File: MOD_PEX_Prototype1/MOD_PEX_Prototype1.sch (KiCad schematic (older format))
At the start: 66 parts, among them CN1 CONN_PANNEL_2X2, CN2 CONN_PANNEL_2X2, J1 RJ45_CHAIN, J2 RJ45_CHAIN, P1 HEADER_3X1, P2 HEADER_5X1, P3 HEADER_5X2, P4 HEADER_2X1, Q1 MMBT3904, Q2 MMBT3904, SW1 SWITCH_HH, U1 LPC111X_LQFP48, U2 AP1117E50G, U3 AP1117E33G, U4 SN75176BDR, X1 10MHz

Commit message: Created BOM with ITEAD template.
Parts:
- removed D2, D3: MMSZ5242B, SOD123, symbol ZENERSMALL
- added D2, D3: MMSZ5242B, SOD123, symbol ZENERsmall
- C1, C3, C7: value 10uF -> 100uF
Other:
- moved on the sheet: C15, C6, C9, CN1, CN2, J1, J2, P1, P3, P4, Q1, Q2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

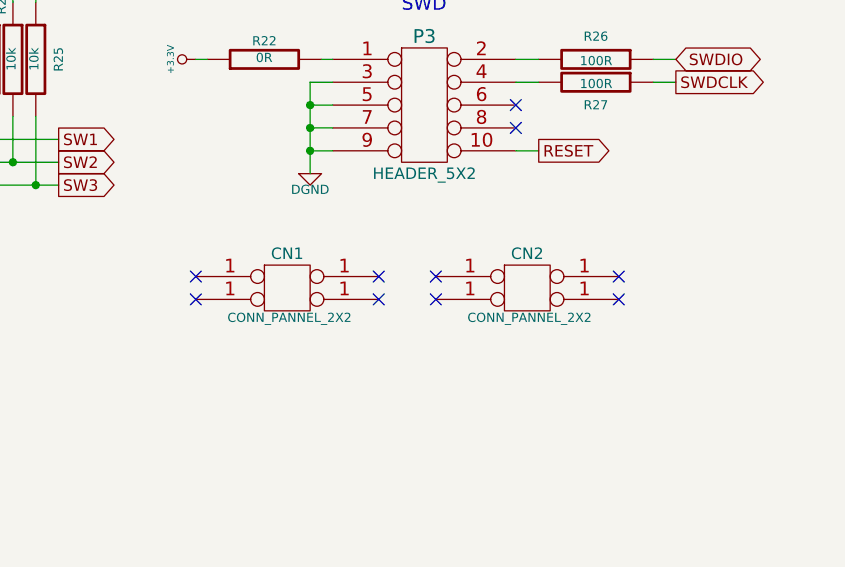
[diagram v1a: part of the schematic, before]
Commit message: Adding metadata to the schematics drawing (fix issue #5) and improving the PCB grounding by attaching CN1 and CN2 to the DGND copper plane (fix issue #4).
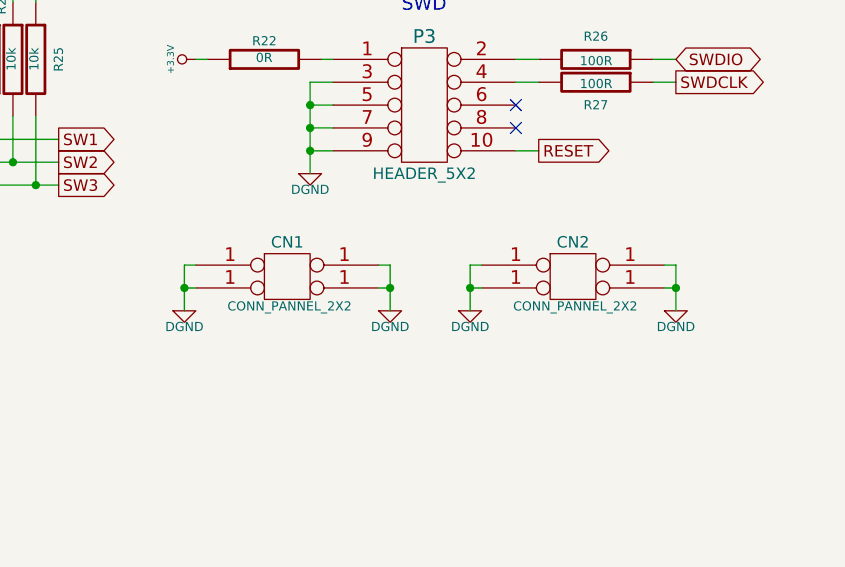
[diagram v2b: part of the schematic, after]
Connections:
- net DGND: now also CN1.1, CN2.1
- no-connect marks 39 -> 31
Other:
- moved on the sheet: CN1, CN2
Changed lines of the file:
@@
 LIBS:MOD_PEX_Prototype1
 LIBS:MOD_PEX_Prototype1-cache
-EELAYER 24 0
+EELAYER 25 0
 EELAYER END
 $Descr A4 11693 8268
 encoding utf-8
 Sheet 1 1
-Title ""
+Title "Control-Chain Expression Pedal for the MOD Project."
 Date "15 apr 2014"
 Rev ""
-Comp ""
+Comp "http://portalmod.com/"
 Comment1 ""
 Comment2 ""
@@
 	3500 1300 3500 1500
 Connection ~ 3500 1400
-NoConn ~ 9200 6250
-NoConn ~ 9200 6350
-NoConn ~ 8400 6250
-NoConn ~ 8400 6350
-NoConn ~ 10250 6250
-NoConn ~ 10250 6350
-NoConn ~ 9450 6250
-NoConn ~ 9450 6350
 $Comp
 L CONN_PANNEL_2X2 CN1
 U 1 1 534AEC1C
-P 8800 6300
-F 0 "CN1" H 8800 6450 50  0000 C CNN
-F 1 "CONN_PANNEL_2X2" H 8810 6170 40  0000 C CNN
-F 2 "CONN_PANNEL" H 8800 6300 60  0001 C CNN
-F 3 "" H 8800 6300 60  0000 C CNN
-	1    8800 6300
+P 8800 6250
+F 0 "CN1" H 8800 6400 50  0000 C CNN
+F 1 "CONN_PANNEL_2X2" H 8810 6120 40  0000 C CNN
+F 2 "CONN_PANNEL" H 8800 6250 60  0001 C CNN
+F 3 "" H 8800 6250 60  0000 C CNN
+	1    8800 6250
 	1    0    0    -1
 $EndComp
@@
 L CONN_PANNEL_2X2 CN2
 U 1 1 534AEC33
-P 9850 6300
-F 0 "CN2" H 9850 6450 50  0000 C CNN
-F 1 "CONN_PANNEL_2X2" H 9860 6170 40  0000 C CNN
-F 2 "CONN_PANNEL" H 9850 6300 60  0001 C CNN
-F 3 "" H 9850 6300 60  0000 C CNN
-	1    9850 6300
+P 10050 6250
+F 0 "CN2" H 10050 6400 50  0000 C CNN
+F 1 "CONN_PANNEL_2X2" H 10060 6120 40  0000 C CNN
+F 2 "CONN_PANNEL" H 10050 6250 60  0001 C CNN
+F 3 "" H 10050 6250 60  0000 C CNN
+	1    10050 6250
 	1    0    0    -1
 $EndComp
@@
 	0    -1   -1   0
 $EndComp
+$Comp
+L DGND #PWR?
+U 1 1 547CBA4C
+P 8350 6400
+F 0 "#PWR?" H 8350 6400 40  0001 C CNN
+F 1 "DGND" H 8350 6330 40  0000 C CNN
+F 2 "" H 8350 6400 60  0000 C CNN
+F 3 "" H 8350 6400 60  0000 C CNN
+	1    8350 6400
+	1    0    0    -1
+$EndComp
+Wire Wire Line
+	8400 6300 8350 6300
+Wire Wire Line
+	8350 6200 8350 6400
+Wire Wire Line
+	8350 6200 8400 6200
+Connection ~ 8350 6300
+$Comp
+L DGND #PWR?
+U 1 1 547CBE36
+P 9250 6400
+F 0 "#PWR?" H 9250 6400 40  0001 C CNN
+F 1 "DGND" H 9250 6330 40  0000 C CNN
+F 2 "" H 9250 6400 60  0000 C CNN
+F 3 "" H 9250 6400 60  0000 C CNN
+	1    9250 6400
+	1    0    0    -1
+$EndComp
+Wire Wire Line
+	9200 6300 9250 6300
+Wire Wire Line
+	9250 6200 9250 6400
+Wire Wire Line
+	9200 6200 9250 6200
+Connection ~ 9250 6300
+$Comp
+L DGND #PWR?
+U 1 1 547CC330
+P 9600 6400
+F 0 "#PWR?" H 9600 6400 40  0001 C CNN
+F 1 "DGND" H 9600 6330 40  0000 C CNN
+F 2 "" H 9600 6400 60  0000 C CNN
+F 3 "" H 9600 6400 60  0000 C CNN
+	1    9600 6400
+	1    0    0    -1
+$EndComp
+$Comp
+L DGND #PWR?
+U 1 1 547CC37D
+P 10500 6400
+F 0 "#PWR?" H 10500 6400 40  0001 C CNN
+F 1 "DGND" H 10500 6330 40  0000 C CNN
+F 2 "" H 10500 6400 60  0000 C CNN
+F 3 "" H 10500 6400 60  0000 C CNN
+	1    10500 6400
+	1    0    0    -1
+$EndComp
+Wire Wire Line
+	10500 6200 10500 6400
+Wire Wire Line
+	10500 6300 10450 6300
+Wire Wire Line
+	10450 6200 10500 6200
+Connection ~ 10500 6300
+Wire Wire Line
+	9650 6300 9600 6300
+Wire Wire Line
+	9600 6200 9600 6400
+Wire Wire Line
+	9600 6200 9650 6200
+Connection ~ 9600 6300
 $EndSCHEMATC

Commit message: updating footprints (to use the ones from the mod-kicad-footprints repository)
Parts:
- C1, C3, C7: footprint CAP_RAD_5MM -> MOD_Footprints_Lib:CAP_RAD_5MM
- C10, C11, C12, C13, C14, C15, C2, C4, C5, C6, C8, C9, R1, R10, R13, R14, R15, R17, R18, R19, R2, R20, R21, R23, R24, R25, R26, R27, R28, R9: footprint SM0603 -> MOD_Footprints_Lib:SM0603
- CN1, CN2: footprint CONN_PANNEL -> MOD_Footprints_Lib:CONN_PANNEL
- D1: footprint DO-214AC(SMA) -> MOD_Footprints_Lib:DO-214AC(SMA)
- D2, D3: footprint SOD123 -> MOD_Footprints_Lib:SOD123
- D4: footprint SOD323 -> MOD_Footprints_Lib:SOD323
- J1, J2: footprint RJ45-RJHSE5084 -> MOD_Footprints_Lib:RJ45-RJHSE5084
- P1: footprint PIN_ARRAY_3X1 -> MOD_Footprints_Lib:PIN_ARRAY_3X1
- P2: footprint PIN_ARRAY_5x1 -> MOD_Footprints_Lib:PIN_ARRAY_5x1
- P3: footprint PIN_ARRAY_5x2 -> MOD_Footprints_Lib:PIN_ARRAY_5x2
- P4: footprint PIN_ARRAY_2X1 -> MOD_Footprints_Lib:PIN_ARRAY_2X1
- Q1, Q2: footprint SOT23 -> MOD_Footprints_Lib:SOT23
- R11, R12, R16, R22, R3, R4, R5, R6, R7, R8: footprint SM0805 -> MOD_Footprints_Lib:SM0805
- RT1: footprint SM2920 -> MOD_Footprints_Lib:SM2920
- SW1: footprint SWITCH_HH_SK-13D26-G-6.5-K-GY -> MOD_Footprints_Lib:SWITCH_HH_SK-13D26-G-6_5-K-GY
- TP1, TP2: footprint SIL-1 -> MOD_Footprints_Lib:SIL-1
- U1: footprint LQFP48 -> MOD_Footprints_Lib:LQFP48
- U2, U3: footprint SOT223_3 -> MOD_Footprints_Lib:SOT223_3
- U4: footprint SO8E -> MOD_Footprints_Lib:SO8E
- X1: footprint HC_49US -> MOD_Footprints_Lib:HC_49US

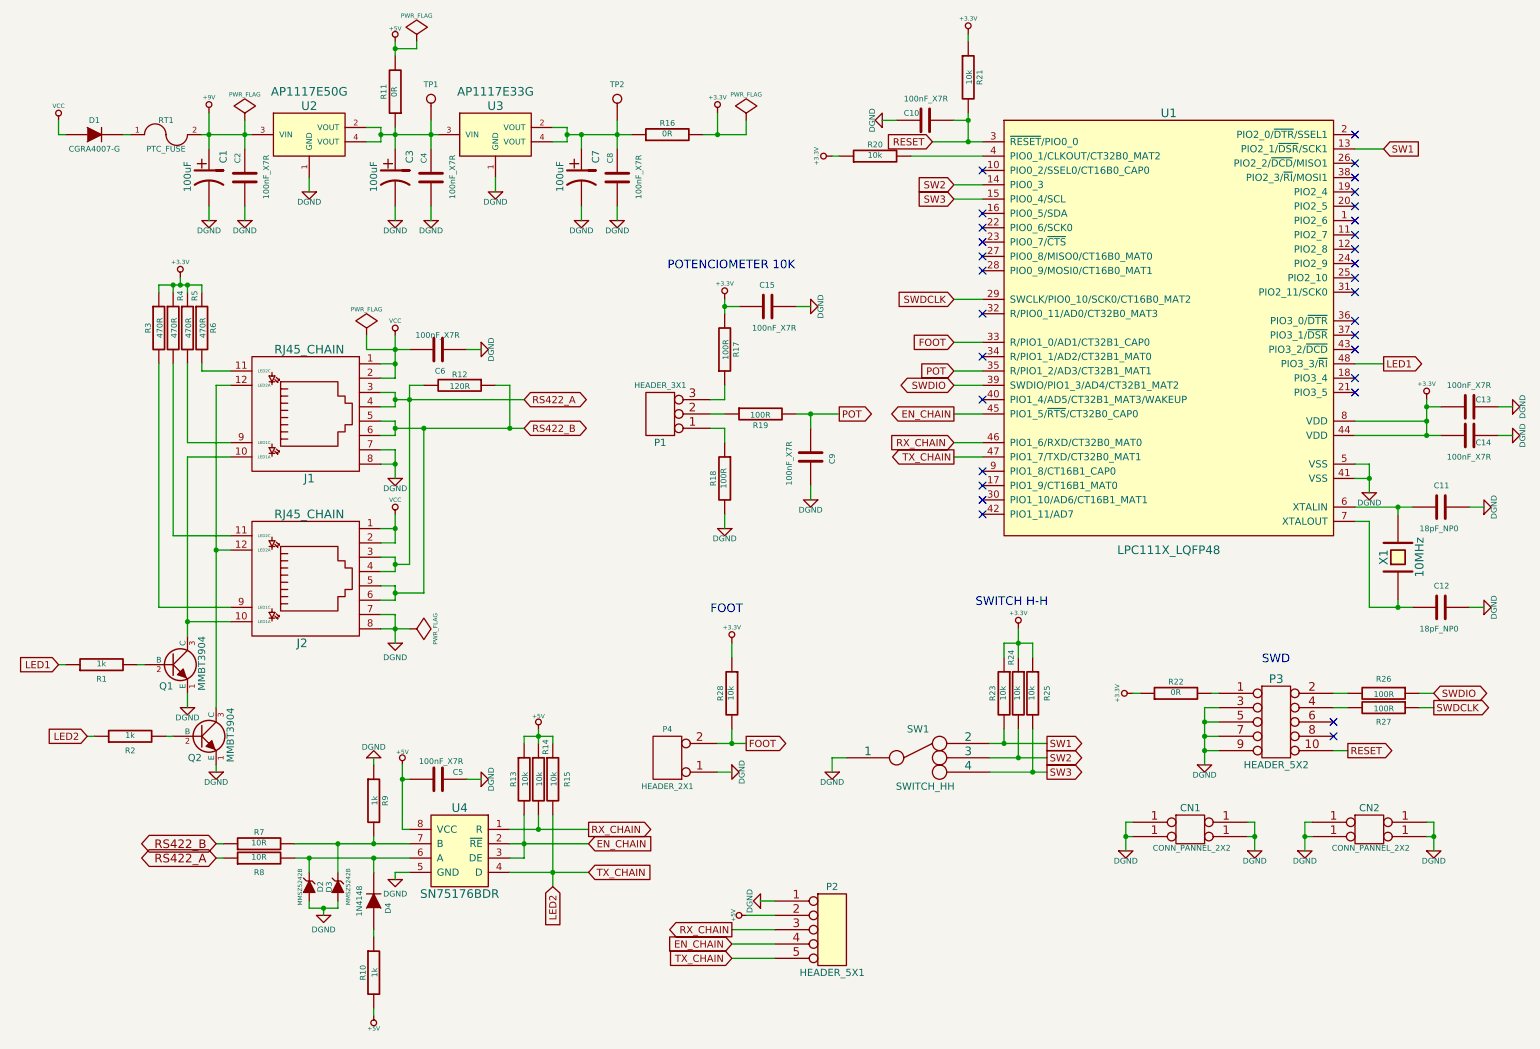
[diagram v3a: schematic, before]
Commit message: wip on issue #7: protect the U4 IC when the board is being debugged Made the necessary changes in the schematics drawing.
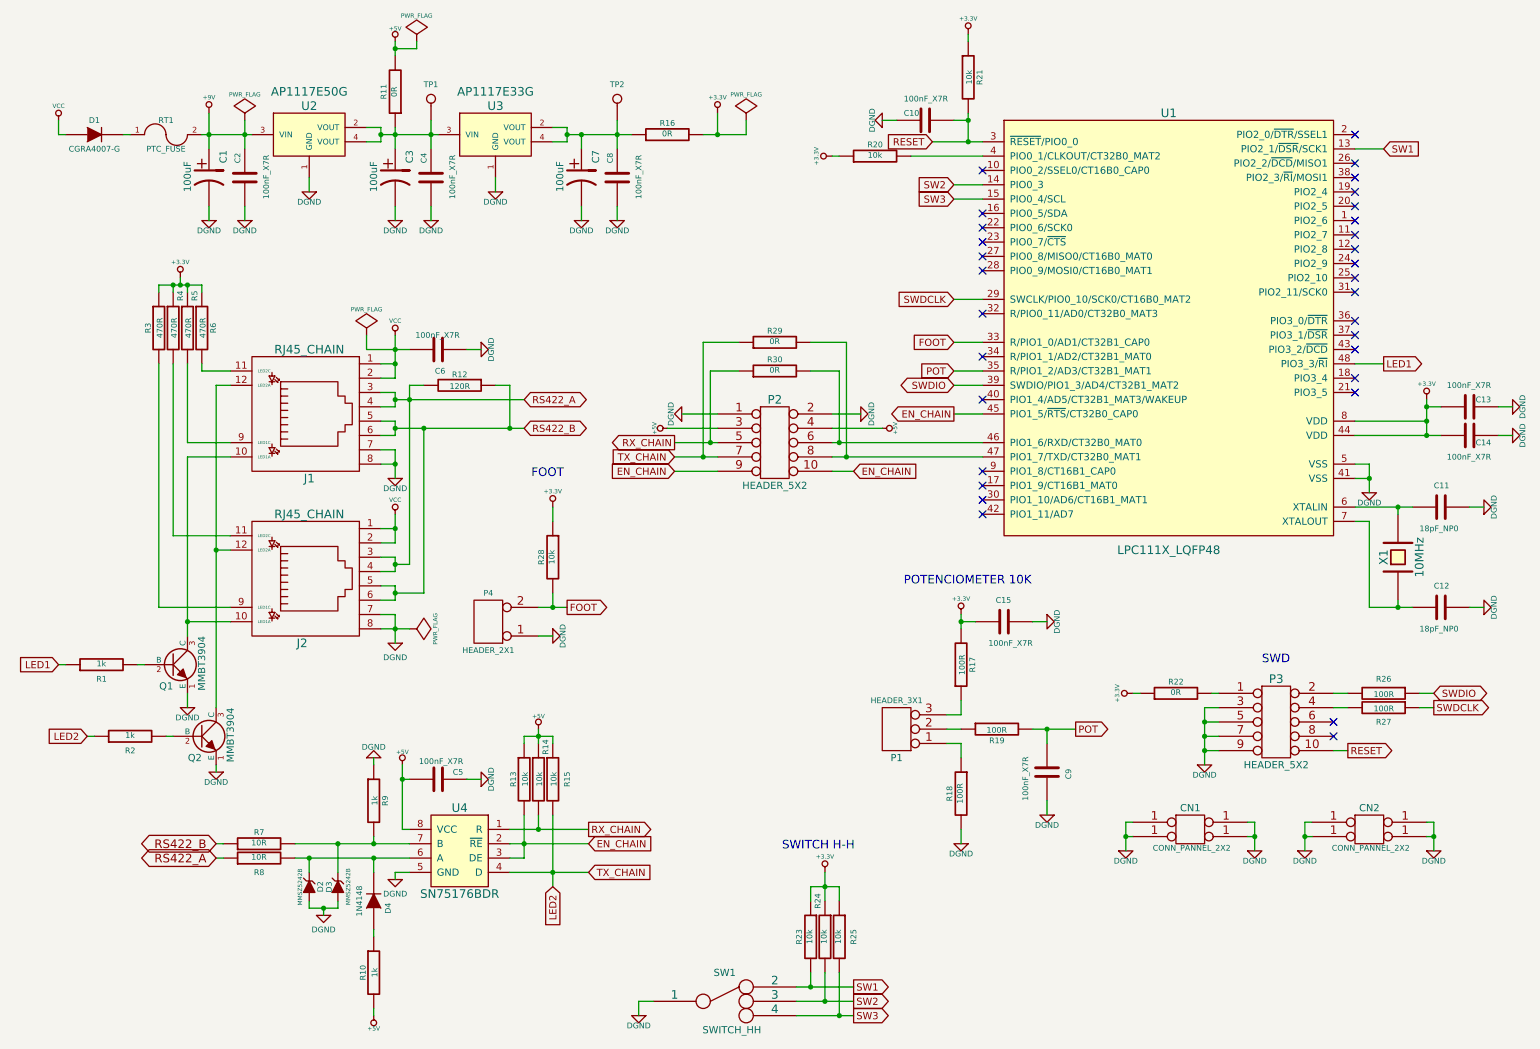
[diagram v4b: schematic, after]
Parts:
- removed P2: HEADER_5X1, MOD_Footprints_Lib:PIN_ARRAY_5x1, symbol CONN_5
- added P2: HEADER_5X2, MOD_Footprints_Lib:PIN_ARRAY_5x2, symbol CONN_5X2
- added R29, R30: 0R, MOD_Footprints_Lib:SM0805, symbol R
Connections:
- net +5V: now also P2.3, P2.4
- net DGND: now also P2.1, P2.2
- net EN_CHAIN: now also P2.10, P2.9
- net LED2: now also P2.7, R29.1; no longer U1.47 (PIO1_7/TXD/CT32B0_MAT1)
- net RX_CHAIN: now also P2.5, R30.1; no longer U1.46 (PIO1_6/RXD/CT32B0_MAT0)
- new net: P2.6, R30.2, U1.46 (PIO1_6/RXD/CT32B0_MAT0)
- new net: P2.8, R29.2, U1.47 (PIO1_7/TXD/CT32B0_MAT1)
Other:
- moved on the sheet: C15, C9, P1, P4, R17, R18, R19, R23, R24, R25, R28, SW1

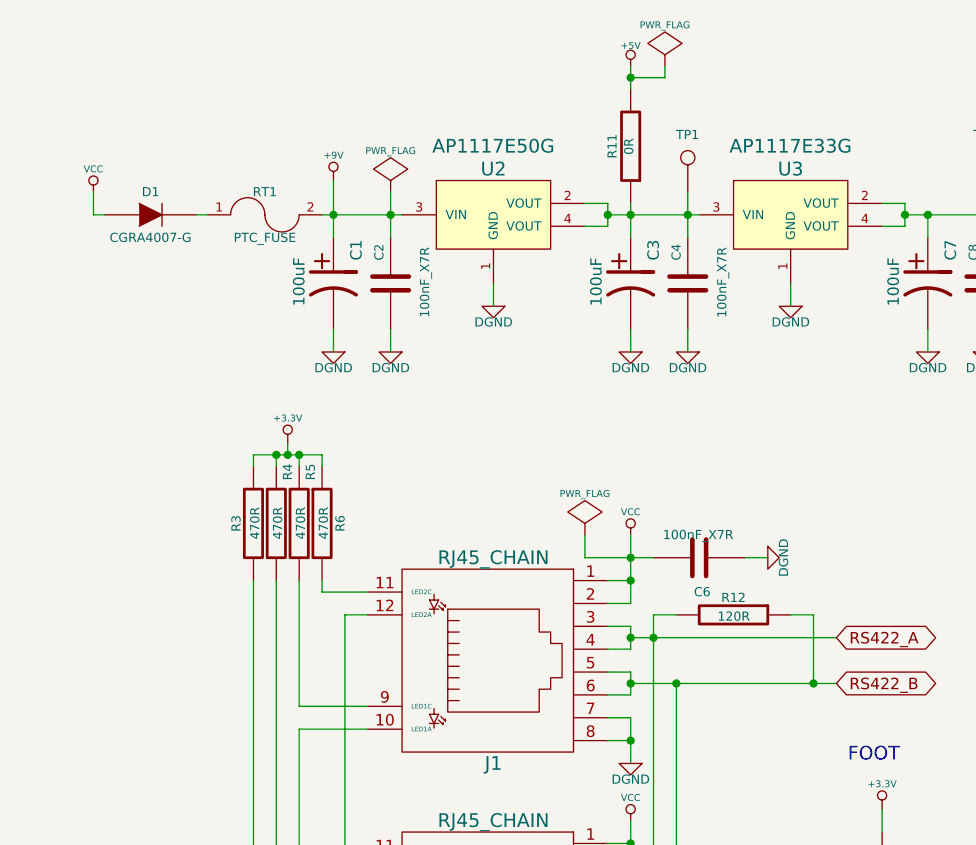
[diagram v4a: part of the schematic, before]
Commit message: wip on issue #9: change footprint of RT1 I'm adding a second footprint so that we have 2 choices of fuse packages we can use: SM2920 or SM1210
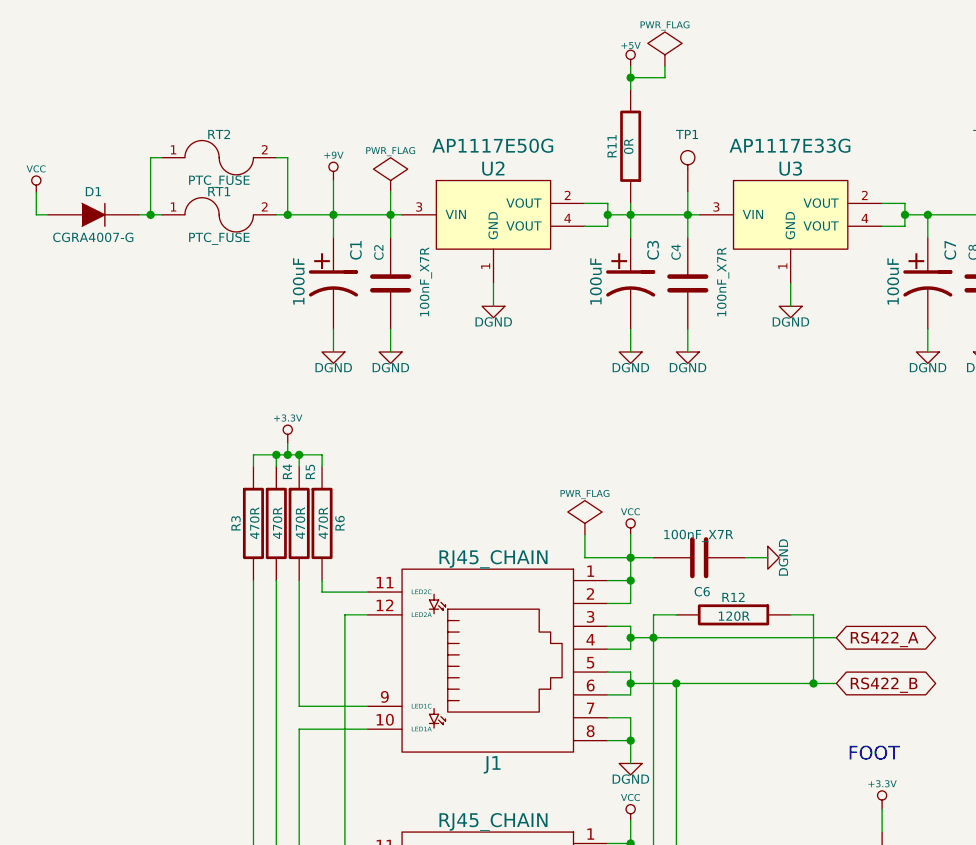
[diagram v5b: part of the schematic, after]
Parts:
- added RT2: PTC_FUSE, MOD_Footprints_Lib:SM2920, symbol FUSE
- RT1: footprint MOD_Footprints_Lib:SM2920 -> MOD_Footprints_Lib:SM1210
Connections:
- net +9V: now also RT2.2
- net at D1.2 (K), RT1.1: now also RT2.1
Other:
- moved on the sheet: D1, RT1
